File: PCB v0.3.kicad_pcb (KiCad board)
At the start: 2 copper layers, 102.5 x 102.5 mm, 67 parts, among them J1 XT60-M, J10 Screw 2.54mm 5P, J11 Screw 2.54mm 5P, J12 Screw 2.54mm 5P, J13 2.54mm 3P, J14 2.54mm 3P, J15 2.54mm 3P, J16 2.54mm 3P, J17 JST-SH 3P, J18 JST-SH 3P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

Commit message: Finished v0.3 SCH
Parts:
- removed C10, C11: 100u 50V (E), Capacitor_THT:CP_Radial_D8.0mm_P3.50mm
- removed D8: Green 0805, LED_SMD:LED_0805_2012Metric_Pad1.15x1.40mm_HandSolder
- removed F3: 500mA 1206, Fuse:Fuse_1206_3216Metric
- removed FB1, FB2, FB3: BLM21PG220, Inductor_SMD:L_0805_2012Metric_Pad1.05x1.20mm_HandSolder
- added R9: 470R 0805, Resistor_SMD:R_0805_2012Metric_Pad1.20x1.40mm_HandSolder, F.Cu at (394.9, 167.8)
- C2: value 1000u 50V (E) -> 0.1u 50V 1206 (C); footprint Capacitor_THT:CP_Radial_D13.0mm_P5.00mm -> Capacitor_SMD:C_1206_3216Metric_Pad1.33x1.80mm_HandSolder
- C4: value 0.1u 50V 1206 (C) -> 100n 50V 1206 (C)
- C6: value 100u 50V (E) -> 1000u 50V (E); footprint Capacitor_THT:CP_Radial_D8.0mm_P3.50mm -> Capacitor_THT:CP_Radial_D13.0mm_P5.00mm
- C7: value 0.1u 50V 1206 (C) -> 470u 50V (E); footprint Capacitor_SMD:C_1206_3216Metric_Pad1.33x1.80mm_HandSolder -> Capacitor_THT:CP_Radial_D10.0mm_P5.00mm
- C9: value 100u 50V (E) -> 0.1u 50V 1206 (C); footprint Capacitor_THT:CP_Radial_D8.0mm_P3.50mm -> Capacitor_SMD:C_1206_3216Metric_Pad1.33x1.80mm_HandSolder
- D2: value 3.3V -> SK1010C; footprint Diode_SMD:Nexperia_CFP3_SOD-123W -> Diode_SMD:D_SMC_Handsoldering
- D3: value SK1010C -> SMAJ6.0A; footprint Diode_SMD:D_SMC_Handsoldering -> Diode_SMD:D_SMA
- D4: value SMAJ6.0A -> Green 0805; footprint Diode_SMD:D_SMA -> LED_SMD:LED_0805_2012Metric_Pad1.15x1.40mm_HandSolder
- F1: value 30A -> 15A
- J10, J7, J8, J9: value Screw 2.54mm 5P -> 2.54mm 3P; footprint TerminalBlock:TerminalBlock_Xinya_XY308-2.54-5P_1x05_P2.54mm_Horizontal -> Connector_PinHeader_2.54mm:PinHeader_1x03_P2.54mm_Vertical
- J11, J12: value Screw 2.54mm 5P -> 2.54mm 5P Terminal Block
- J13, J14, J15, J16: value 2.54mm 3P -> 2.54mm 5P Terminal Block; footprint Connector_PinHeader_2.54mm:PinHeader_1x03_P2.54mm_Vertical -> TerminalBlock:TerminalBlock_Xinya_XY308-2.54-5P_1x05_P2.54mm_Horizontal
- U1: moved to F.Cu
- moved C8 485.0 mm to (401.4, 127.0)
- moved C6 455.6 mm to (370.9, 144.1)
- moved C5 437.7 mm to (384.2, 148.5)
- moved C9 437.4 mm to (352.3, 168.7)
- moved J17 435.2 mm to (361.8, 125.4)
- moved J18 435.2 mm to (361.8, 131.6)
- moved J19 435.2 mm to (361.8, 137.9)
- moved J20 435.2 mm to (361.8, 144.1)
- moved J21 435.2 mm to (361.8, 150.4)
- moved J22 435.2 mm to (361.8, 156.6)
- moved C7 426.5 mm to (384.2, 160.0)
- moved J13 423.0 mm to (393.8, 60.6)
- moved TP1 421.1 mm to (399.0, 165.9)
- moved TP2 421.1 mm to (399.0, 169.5)
- moved TP3 421.1 mm to (402.6, 165.9)
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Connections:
- A1 pad 35: Net-(A1-ADC_VREF) -> +3V3
- A1 pad 39: Net-(A1-VSYS) -> +5.1V
- C2 pad 1: +BATT -> +5.1V
- C3 pad 1: Net-(A1-ADC_VREF) -> +5.1V
- C4 pad 1: /ADC_IN -> +3V3
- C5 pad 1: Net-(D3-K) -> +7.5V
- C6 pad 1: +5.1V -> +12V
- C7 pad 1: +5.1V -> Net-(D2-K)
- C8 pad 1: +7.5V -> +5.1V
- C9 pad 1: +7.5V -> /ADC_IN
- D2 pad 1: /ADC_IN -> Net-(D2-K)
- D2 pad 2: GND -> +12V
- D3 pad 1: Net-(D3-K) -> +5.1V
- D3 pad 2: +12V -> GND
- D4 pad 1: +5.1V -> Net-(D4-K)
- D4 pad 2: GND -> +BATT
- D5 pad 2: +BATT -> +12V
- D6 pad 2: +12V -> +7.5V
- D7 pad 2: +7.5V -> +5.1V
- F2 pad 1: Net-(F2-Pad1) -> Net-(U1-+VDC)
- J10 pad 2: /REV_3 -> +7.5V
- J10 pad 3: /BLDC_3 -> /SERVO_3
- J11 pad 2: /REV_4 -> /REV_0
- J11 pad 3: /BLDC_4 -> /BLDC_0
- J12 pad 2: /REV_5 -> /REV_1
- J12 pad 3: /BLDC_5 -> /BLDC_1
- J13 pad 2: +7.5V -> /REV_2
- J13 pad 3: /SERVO_0 -> /BLDC_2
- J14 pad 2: +7.5V -> /REV_3
- J14 pad 3: /SERVO_1 -> /BLDC_3
- J15 pad 2: +7.5V -> /REV_4
- J15 pad 3: /SERVO_2 -> /BLDC_4
- J16 pad 2: +7.5V -> /REV_5
- J16 pad 3: /SERVO_3 -> /BLDC_5
- J2 pad 2: Net-(FB1-Pad1) -> +5.1V
- J2 pad 4: Net-(FB1-Pad1) -> +5.1V
- J7 pad 2: /REV_0 -> +7.5V
- J7 pad 3: /BLDC_0 -> /SERVO_0
- J8 pad 2: /REV_1 -> +7.5V
- J8 pad 3: /BLDC_1 -> /SERVO_1
- J9 pad 2: /REV_2 -> +7.5V
- J9 pad 3: /BLDC_2 -> /SERVO_2
- R4 pad 2: Net-(D5-K) -> Net-(D4-K)
- R5 pad 1: GND -> Net-(R5-Pad1)
- R5 pad 2: Net-(R4-Pad1) -> Net-(D5-K)
- R6 pad 2: Net-(D6-K) -> Net-(R4-Pad1)
- R7 pad 2: Net-(D7-K) -> Net-(R5-Pad1)
- R8 pad 2: Net-(D8-K) -> Net-(D6-K)
- TP5 pad 1: /ADC_IN -> +5.1V
- TP6 pad 1: +5.1V -> /ADC_IN
- U1 pad 1: +5.1V -> Net-(U1-+VDC)
- U1 pad 4: Net-(D3-K) -> Net-(D2-K)

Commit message: Laid out power circuitry
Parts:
- F1: footprint Fuse:FuseHolder_Blade_ATO_Littelfuse_FLR_178.6165 -> Fuse:Fuse_Blade_ATO_directSolder
- moved H2 317.5 mm to (107.4, 32.0)
- moved H3 295.2 mm to (107.4, 127.5)
- moved J16 286.9 mm to (107.9, 110.9), turned to -90 degrees
- moved J15 286.5 mm to (107.9, 96.4), turned to -90 degrees
- moved J14 286.1 mm to (107.9, 82.0), turned to -90 degrees
- moved J13 286.0 mm to (107.9, 67.5), turned to -90 degrees
- moved J11 285.9 mm to (107.9, 38.5), turned to -90 degrees
- moved J12 285.9 mm to (107.9, 53.0), turned to -90 degrees
- moved D2 271.1 mm to (133.9, 47.4), turned to 180 degrees
- moved C7 270.1 mm to (134.7, 56.6), turned to 180 degrees
- moved C6 267.8 mm to (119.1, 52.8), turned to -90 degrees
- moved J10 266.5 mm to (145.0, 46.2), turned to 90 degrees
- moved C2 262.7 mm to (145.1, -2.89)
- moved C3 262.7 mm to (145.1, 0.46)
- moved C4 262.7 mm to (145.1, 3.81)
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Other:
- board size 102.5 x 102.5 mm -> 95.5 x 102.5 mm

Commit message: Finished laying out
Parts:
- F2: footprint Fuse:Fuse_1206_3216Metric -> Fuse:Fuse_1812_4532Metric_Pad1.30x3.40mm_HandSolder
- moved TP5 130.3 mm to (155.7, 127.3)
- moved D3 129.3 mm to (148.8, 120.0), turned to -90 degrees
- moved C3 126.3 mm to (161.8, 125.7), turned to 90 degrees
- moved F2 126.0 mm to (144.0, 120.0), turned to 90 degrees
- moved R2 121.5 mm to (161.0, 104.1)
- moved R3 116.2 mm to (161.0, 101.6), turned to 180 degrees
- moved J22 114.4 mm to (153.4, 109.5)
- moved J21 112.9 mm to (153.4, 101.7)
- moved C4 111.7 mm to (161.8, 114.3), turned to 90 degrees
- moved J20 111.4 mm to (153.4, 93.9)
- moved TP2 110.8 mm to (158.2, 113.5)
- moved J19 109.9 mm to (153.4, 86.2)
- moved J18 108.3 mm to (153.4, 78.4)
- moved J17 106.8 mm to (153.4, 70.6)
- moved C9 102.4 mm to (161.8, 108.2), turned to -90 degrees
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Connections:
- A1 pad 33: unconnected-(A1-AGND-Pad33) -> GND

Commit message: Power planes, began routing
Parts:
- moved J17 18.2 mm to (148.6, 88.1), turned to -90 degrees
- moved D4 17.6 mm to (171.2, 72.6)
- moved D5 17.6 mm to (166.1, 72.6)
- moved D6 17.6 mm to (161.0, 72.6)
- moved D7 17.6 mm to (156.0, 72.6)
- moved J19 16.7 mm to (148.6, 102.1), turned to -90 degrees
- moved R9 16.3 mm to (188.5, 72.6), turned to -90 degrees
- moved J18 15.3 mm to (141.6, 88.1), turned to -90 degrees
- moved J21 15.2 mm to (148.5, 116.1), turned to -90 degrees
- moved J20 14.4 mm to (141.6, 102.1), turned to -90 degrees
- moved J22 13.6 mm to (141.5, 116.1), turned to -90 degrees
- moved TP1 11.7 mm to (180.6, 44.7)
- moved R8 11.2 mm to (186.4, 72.6), turned to -90 degrees
- moved U1 9.56 mm to (127.0, 102.6)
- moved A1 9.56 mm to (171.2, 114.1)
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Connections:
- A1 pad 21: /REV_5 -> /REV_0
- A1 pad 22: /BLDC_5 -> /BLDC_0
- A1 pad 4: /REV_4 -> /BLDC_5
- A1 pad 5: /BLDC_4 -> /REV_5
- A1 pad 6: /REV_0 -> /BLDC_4
- A1 pad 7: /BLDC_0 -> /REV_4
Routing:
- net /REV_1: track 0.00 -> 93.8 mm, vias 0 -> 1
- net /BLDC_1: track 0.00 -> 93.0 mm, vias 0 -> 1
- net /REV_2: track 0.00 -> 91.0 mm, vias 0 -> 1
- net /BLDC_2: track 0.00 -> 90.1 mm, vias 0 -> 1
- net /REV_3: track 0.00 -> 87.1 mm, vias 0 -> 1
- net /BLDC_3: track 0.00 -> 86.2 mm, vias 0 -> 1
- net /REV_4: track 0.00 -> 84.2 mm, vias 0 -> 1
- net /REV_5: track 0.00 -> 83.7 mm, vias 0 -> 1
- net /BLDC_4: track 0.00 -> 83.4 mm, vias 0 -> 1
- net /BLDC_5: track 0.00 -> 82.0 mm, vias 0 -> 1
- net /BLDC_0: track 0.00 -> 76.2 mm, vias 0 -> 3
- net /REV_0: track 0.00 -> 75.4 mm, vias 0 -> 3
- net /SERVO_1: track 0.00 -> 61.3 mm, vias 0 -> 1
- net /SERVO_3: track 0.00 -> 61.0 mm, vias 0 -> 1
- net /SERVO_0: track 0.00 -> 60.3 mm, vias 0 -> 1
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- added copper zone on F.Cu, net +12V
- added copper zone on F.Cu, net +5.1V
- added copper zone on F.Cu, net +7.5V
- added copper zone on F.Cu, net +BATT
- added copper zone on B.Cu, net GND
- added copper zone on F.Cu, net Net-(D2-K)
- added copper zone on F.Cu, net Net-(J1-Pin_2)
- added copper zone on F.Cu, net Net-(Q1-D)
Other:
- board size 95.5 x 102.5 mm -> 99.6 x 102.5 mm

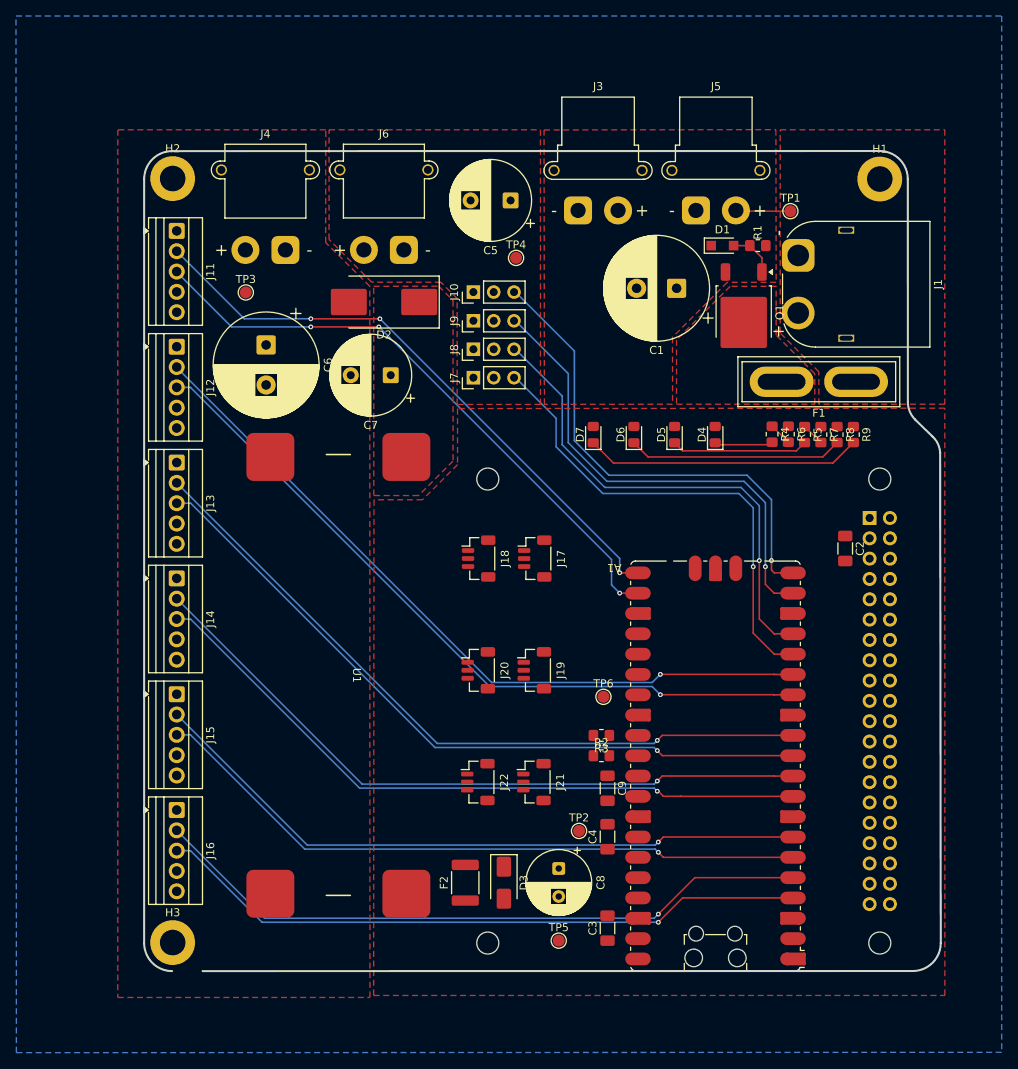
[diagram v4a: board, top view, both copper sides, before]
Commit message: Finished layout and routing. Begun documentation
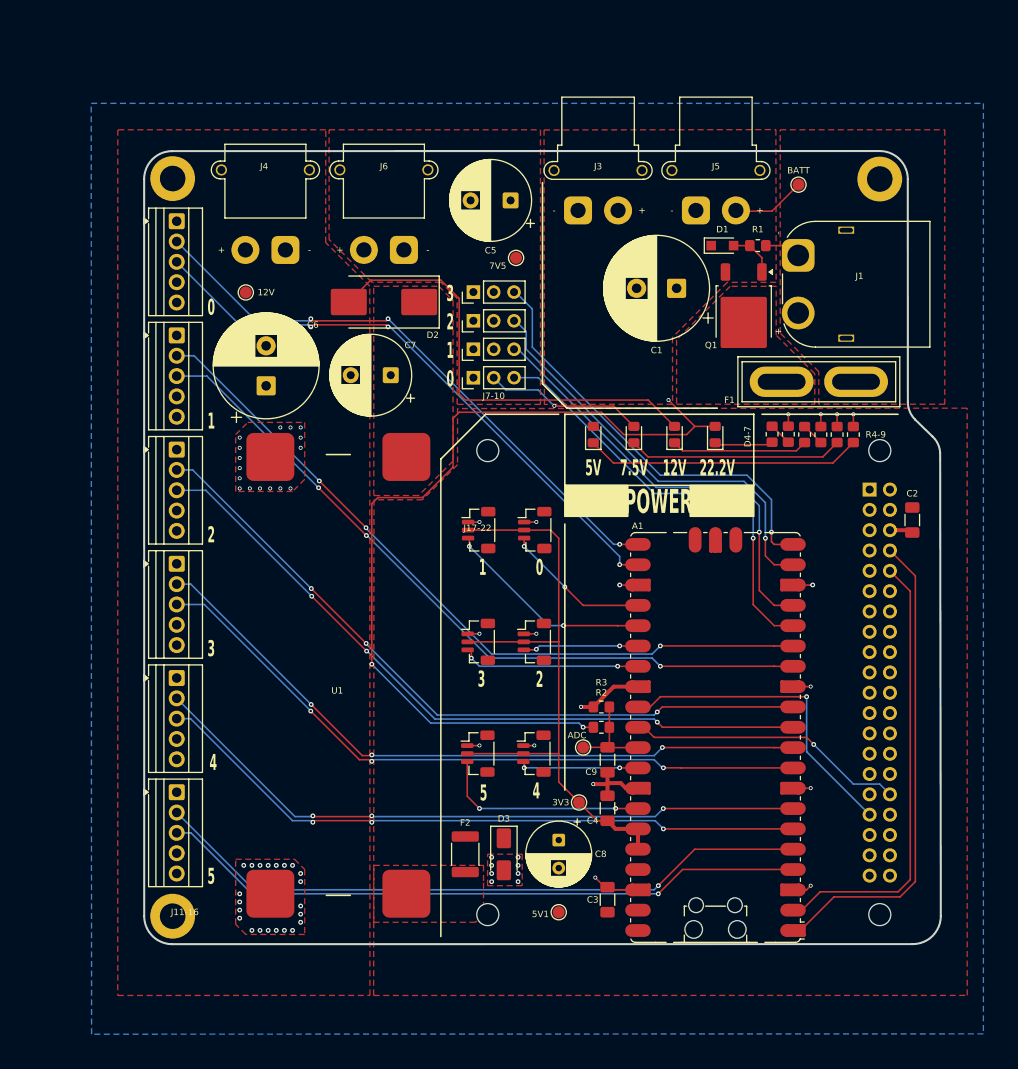
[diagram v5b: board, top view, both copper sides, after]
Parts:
- moved C2 9.11 mm to (195.8, 83.3)
- moved TP6 6.83 mm to (154.7, 111.8)
- moved C6 5.11 mm to (115.1, 66.5), turned to 90 degrees
- moved A1 3.56 mm to (171.2, 110.5)
- moved J17 3.56 mm to (148.6, 84.6)
- moved J18 3.56 mm to (141.6, 84.6)
- moved R3 3.56 mm to (157.0, 106.7)
- moved TP2 3.56 mm to (154.2, 118.6)
- moved C4 3.56 mm to (157.7, 119.4)
- moved C8 3.56 mm to (151.6, 123.3)
- moved C9 3.56 mm to (157.7, 113.3)
- moved D3 3.56 mm to (144.8, 125.1)
- moved F2 3.56 mm to (140.0, 125.1)
- moved J19 3.56 mm to (148.6, 98.6)
- moved J2 3.56 mm to (191.8, 103.6)
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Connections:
- A1 pad 24: /ENC_2 -> /ENC_0
- A1 pad 26: /ENC_0 -> /ENC_2
- J17 pad 2: +5.1V -> +3V3
- J18 pad 2: +5.1V -> +3V3
- J19 pad 2: +5.1V -> +3V3
- J20 pad 2: +5.1V -> +3V3
- J21 pad 2: +5.1V -> +3V3
- J22 pad 2: +5.1V -> +3V3
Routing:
- net +BATT: track 6.85 -> 117.7 mm, vias 0 -> 3
- net +3V3: track 0.00 -> 79.9 mm
- net /UART_TX: track 0.00 -> 60.5 mm
- net GND: track 0.00 -> 57.1 mm, vias 0 -> 64
- net +12V: track 0.00 -> 56.4 mm
- net /UART_RX: track 0.00 -> 55.9 mm
- net /PICO_INT: track 0.00 -> 39.6 mm, vias 0 -> 1
- net /PICO_EN: track 0.00 -> 35.0 mm, vias 0 -> 1
- net /ENC_5: track 0.00 -> 26.3 mm, vias 0 -> 2
- net /ENC_1: track 0.00 -> 26.3 mm, vias 0 -> 2
- net /ENC_3: track 0.00 -> 22.7 mm, vias 0 -> 2
- net +7.5V: track 0.00 -> 20.0 mm, vias 0 -> 1
- net /ENC_0: track 0.00 -> 18.3 mm, vias 0 -> 2
- net /ENC_4: track 0.00 -> 15.1 mm, vias 0 -> 2
- net /ENC_2: track 0.00 -> 14.5 mm, vias 0 -> 2
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- added copper zone on F.Cu, net GND
- added copper zone on F.Cu, net Net-(U1-+VDC)
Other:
- board size 99.6 x 102.5 mm -> 99.6 x 99.1 mm
- board text added: "0"
- board text added: "1"
- board text added: "12V"
- board text added: "2"
- board text added: "22.2V"
- board text added: "3"
- board text added: "3V3"
- board text added: "4"
- board text added: "5"
- board text added: "5V"
- board text added: "5V1"
- board text added: "7.5V"
- board text added: "7V5"
- board text added: "ADC"
- board text added: "BATT"
- board text added: "D4-7"
- board text added: "Designed by Ilo Japar"
- board text added: "HKU MARTIANS"
- board text added: "J11-16"
- board text added: "J17-22"
- board text added: "J7-10"
- board text added: "POWER"
- board text added: "Prototype Rover PCB v0.3 rev A"
- board text added: "R4-9"
